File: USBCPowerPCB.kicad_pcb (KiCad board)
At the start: 2 copper layers, 67.9 x 62.5 mm, 105 parts, among them IC2 TPS56A37RPAR, J1 USB_C_Receptacle_PowerOnly_6P, J10 GND_BANANA_OUT, J2 CC, J3 12V_OUT, J4 5V_ISO, J5 5V_OUT, J6 12V_OUT_PIN, J7 5V_ISO_PIN, J8 5V_OUT_PIN, J9 12V_BANANA_OUT, Q1 IRF9358TRPBF, Q2 BSL308PEH6327XTSA1, U1 TVS2200DRV, U2 CYPD3177-24LQXQT, U3 TPS562231DRLR, U4 TPS2116DRL, U5 TBA2-2411

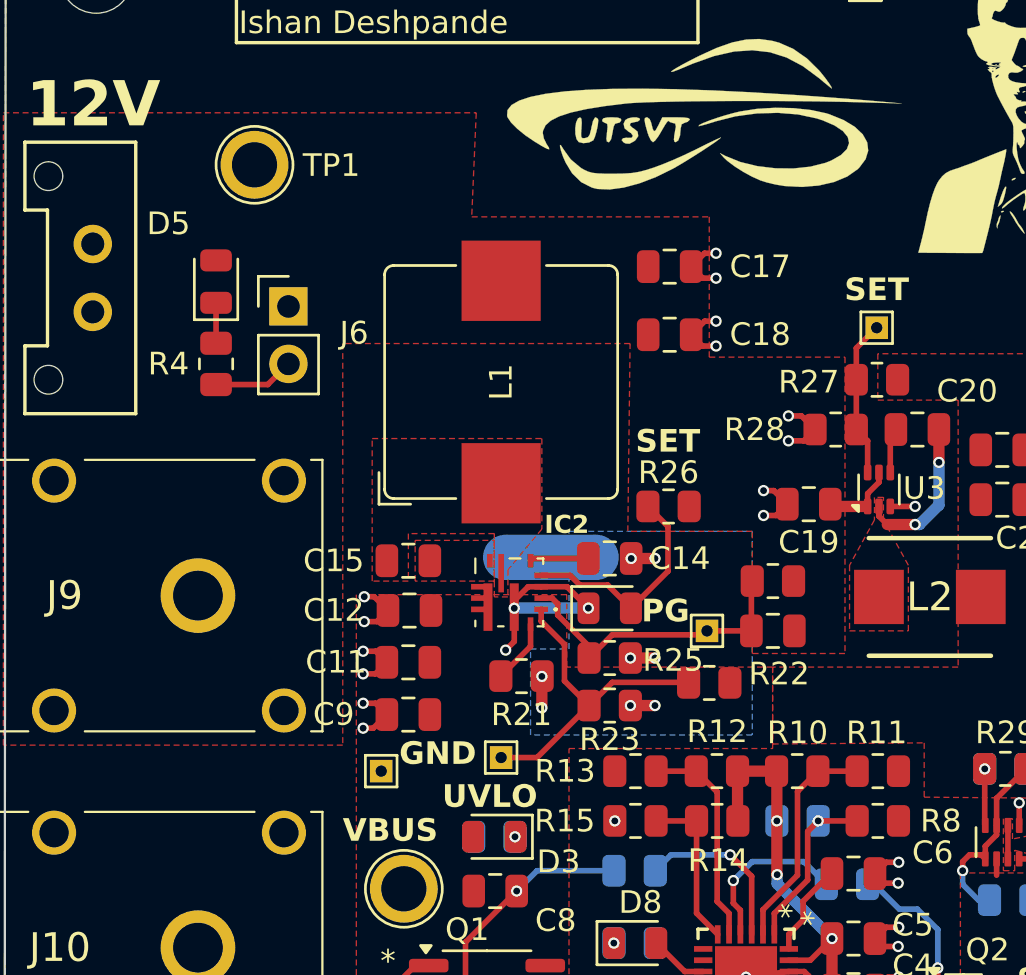
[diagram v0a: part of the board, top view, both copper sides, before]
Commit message: addressed most of the review shit except the TVS/overcurrent protection on the 5V output
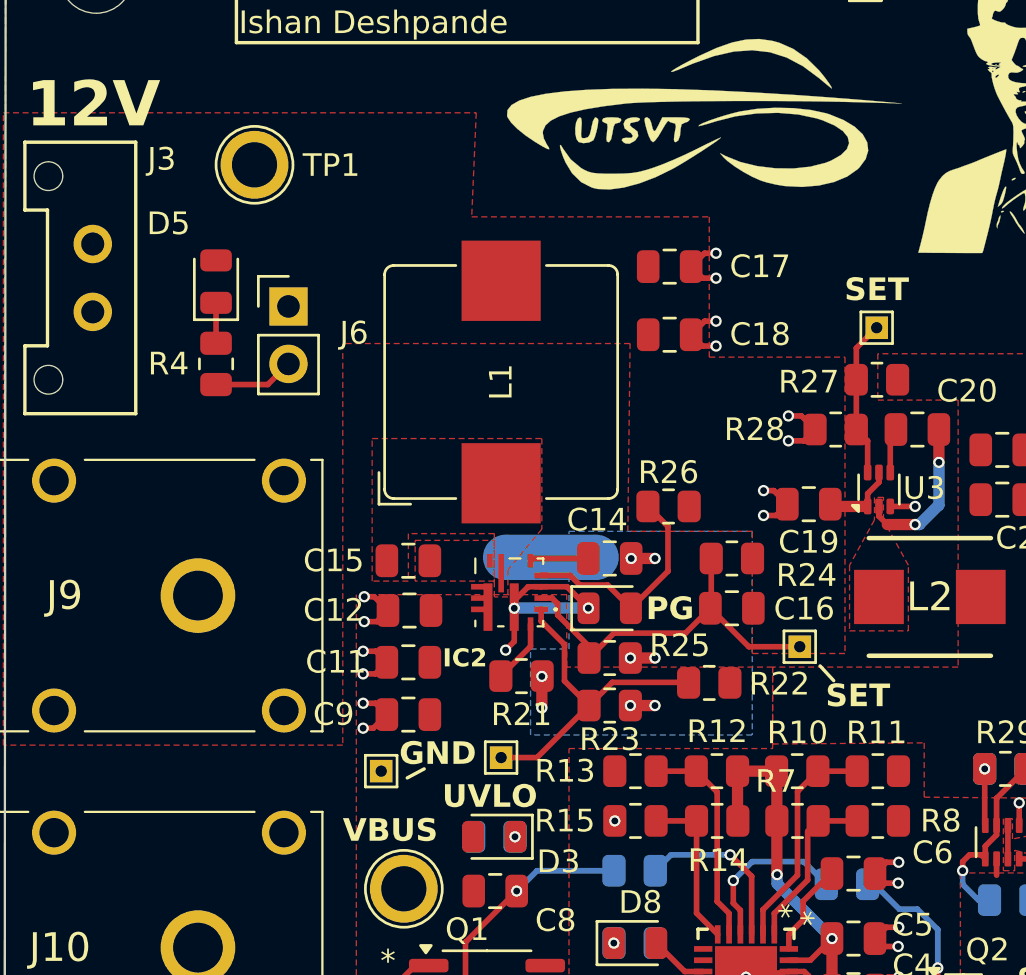
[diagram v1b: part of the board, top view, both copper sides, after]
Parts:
- R7: moved to F.Cu
- moved TP16 4.16 mm to (145.2, 116.7)
- moved R24 2.07 mm to (142.2, 112.8)
- moved C16 2.07 mm to (142.2, 115.0)
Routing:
- net /12V Buck Converter/FB: track 13.1 -> 16.4 mm
- net /Power Delivery Controller/VBUS_MIN: vias 1 -> 0
- net +3.3V: vias 4 -> 3

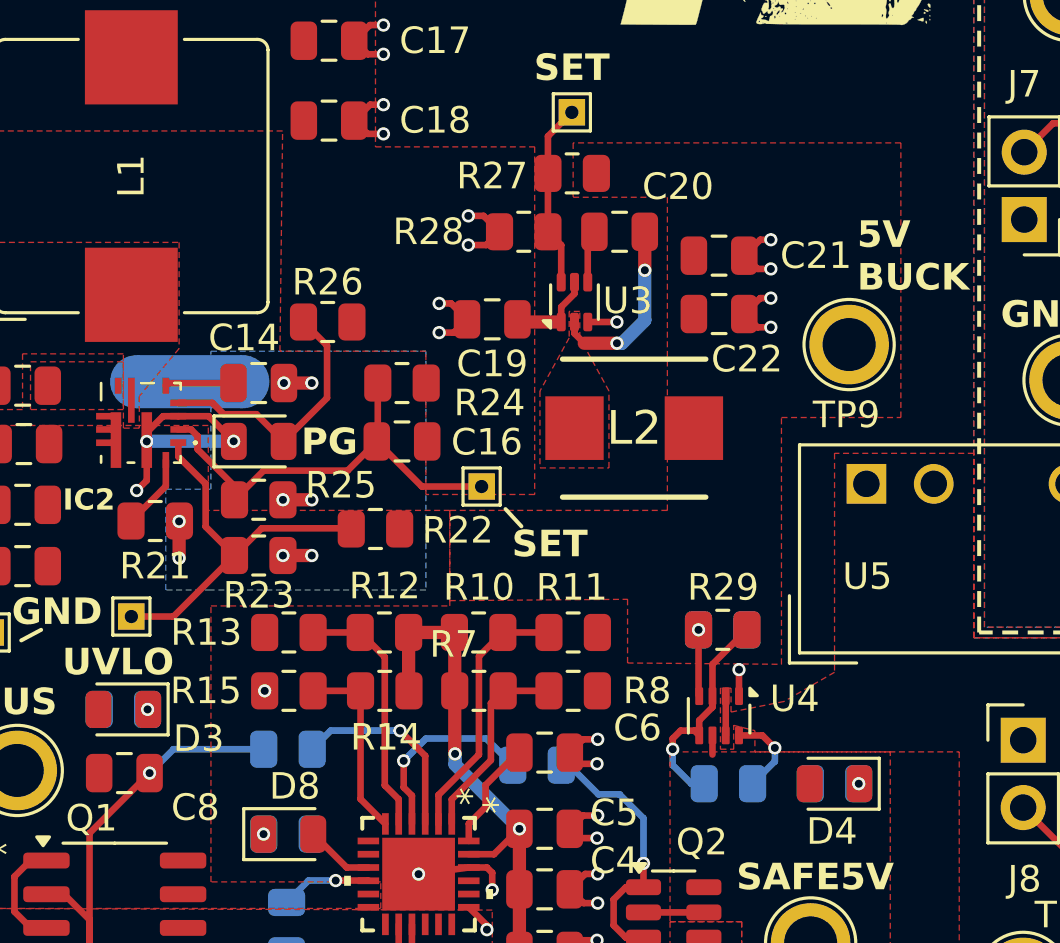
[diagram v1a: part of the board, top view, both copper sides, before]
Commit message: added fuse to protect 5V buck converter output
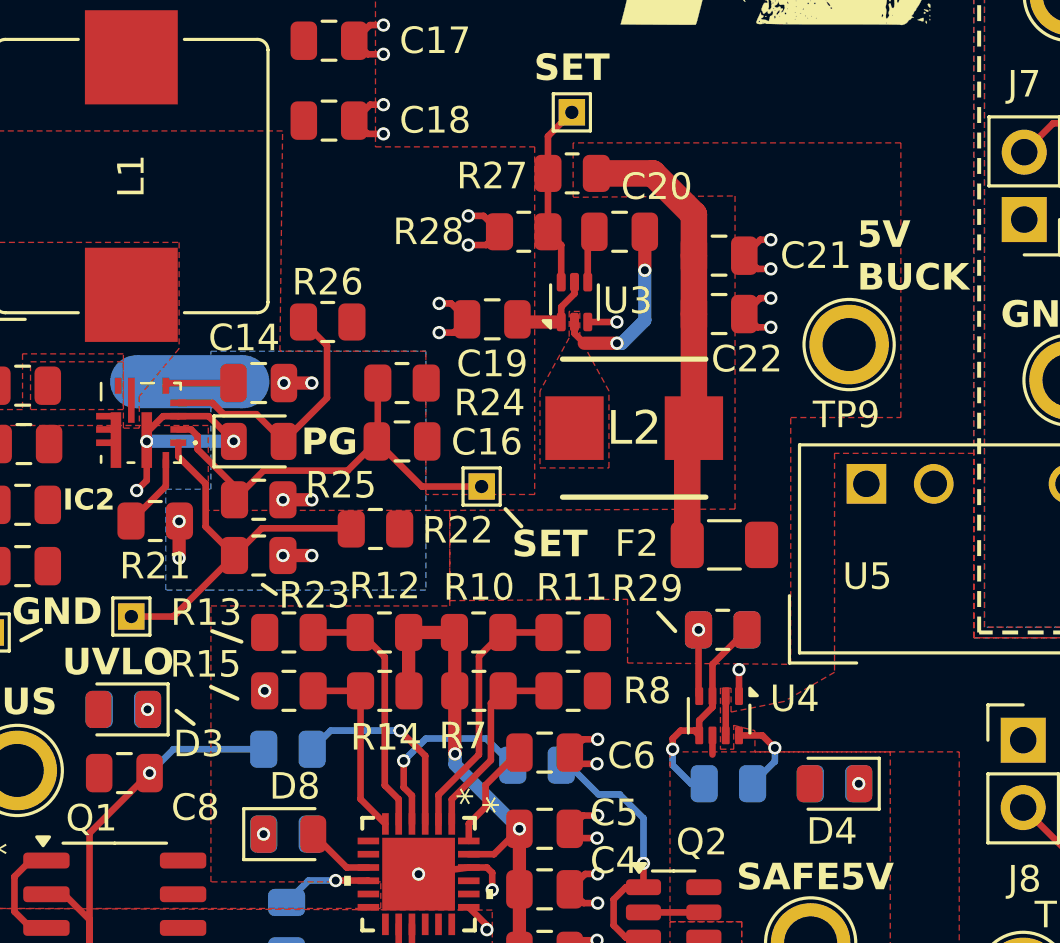
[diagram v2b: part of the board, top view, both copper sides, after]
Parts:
- added F2: 0ZCJ0100FF2E, Fuse:Fuse_1206_3216Metric, F.Cu at (154.3, 118.9)
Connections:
- C21 pad 1: /5V_BUCK -> Net-(C21-Pad1)
- C22 pad 1: /5V_BUCK -> Net-(C21-Pad1)
- L2 pad 2: /5V_BUCK -> Net-(C21-Pad1)
- R27 pad 1: /5V_BUCK -> Net-(C21-Pad1)
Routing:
- net Net-(C21-Pad1): track 0.00 -> 16.9 mm

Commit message: i am jesus christ in the flesh.
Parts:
- moved H2 0.20 mm to (114.1, 141.6)
- moved H4 0.10 mm to (173.8, 141.6)
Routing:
- net Net-(Q1A-G): track 22.2 -> 20.9 mm
- net GND: track 76.0 -> 75.1 mm
- net /Power Delivery Controller/FLIP: track 3.43 -> 3.98 mm
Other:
- board size 67.9 x 62.5 mm -> 67.8 x 62.5 mm

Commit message: i am not jesus christ...
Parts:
- J1: footprint UTSVT_Connectors:TYPEC31M17 -> UTSVT_Connectors:CUI_UJ20-C-H-C-4-SMT-TR
- moved D1 2.90 mm to (149.7, 138.8)
- moved J2 2.90 mm to (149.5, 142.9)
- moved J1 0.77 mm to (142.1, 143.3)
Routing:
- net GND: track 75.1 -> 67.0 mm, vias 48 -> 45
- net /CC2: track 28.3 -> 23.0 mm, vias 2 -> 3
- net /CC1: track 23.8 -> 21.6 mm, vias 2 -> 3
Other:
- outline, holes or cut-outs redrawn
- board text added: "CC"
